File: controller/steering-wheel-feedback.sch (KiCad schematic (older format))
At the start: 6 parts, among them J23 CONN_01X02

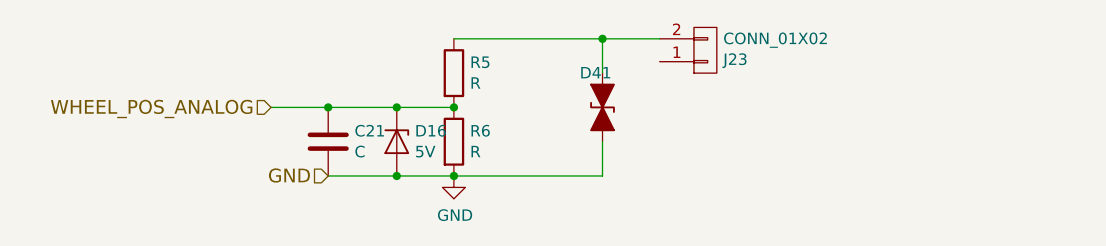
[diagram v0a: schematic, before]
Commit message: add comments with fixes I had to make
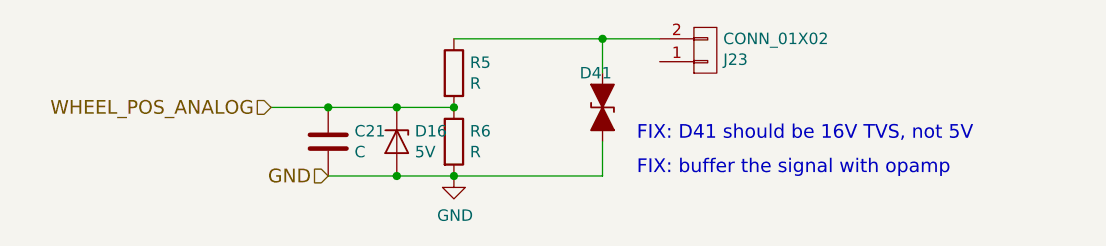
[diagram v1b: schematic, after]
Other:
- note added: "FIX: D41 should be 16V TVS, not 5V"
- note added: "FIX: buffer the signal with opamp"
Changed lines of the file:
@@
 Wire Wire Line
 	5700 3750 5700 3600
+Text Notes 5850 3600 0    60   ~ 0
+FIX: D41 should be 16V TVS, not 5V
+Text Notes 5850 3750 0    60   ~ 0
+FIX: buffer the signal with opamp
 $EndSCHEMATC
